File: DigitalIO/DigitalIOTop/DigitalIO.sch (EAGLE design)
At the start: 9 parts, among them K1 HF46105, K2 HF46105, K3 HF46105, K4 HF46105, Q1 691131710002, Q2 691131710002, Q3 691131710002, Q4 691131710002, X1 87438-06

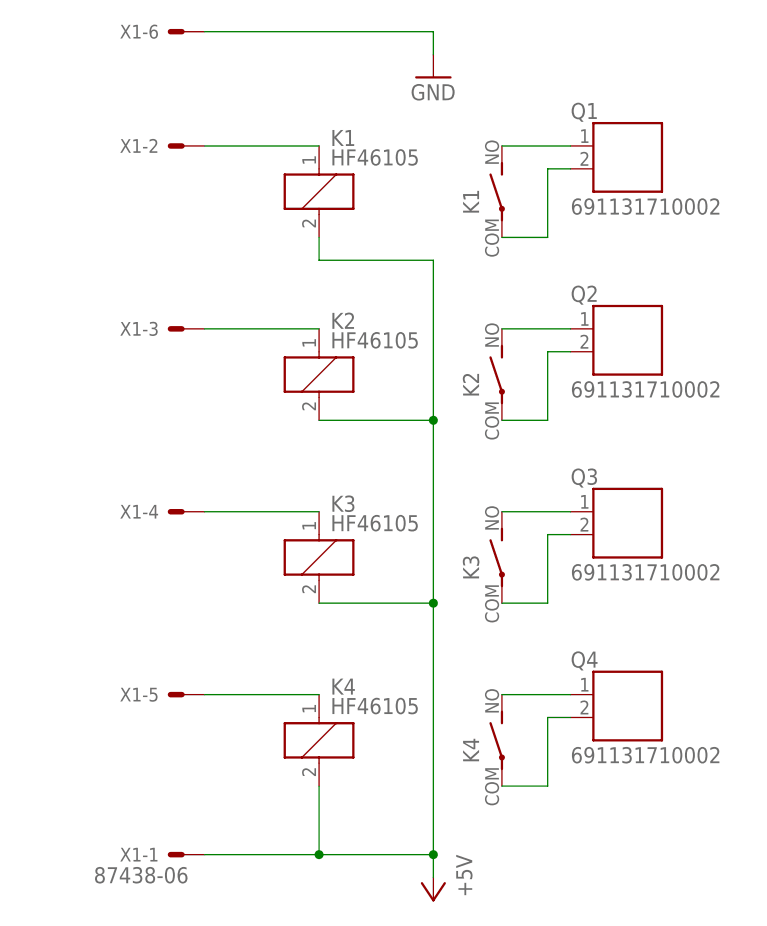
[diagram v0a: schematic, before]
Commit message: Rework to operate with 5V only. Add INT and RESET signals.
Signed-off-by: Alexander Falkenstern <alexander.falkenstern@gmail.com>
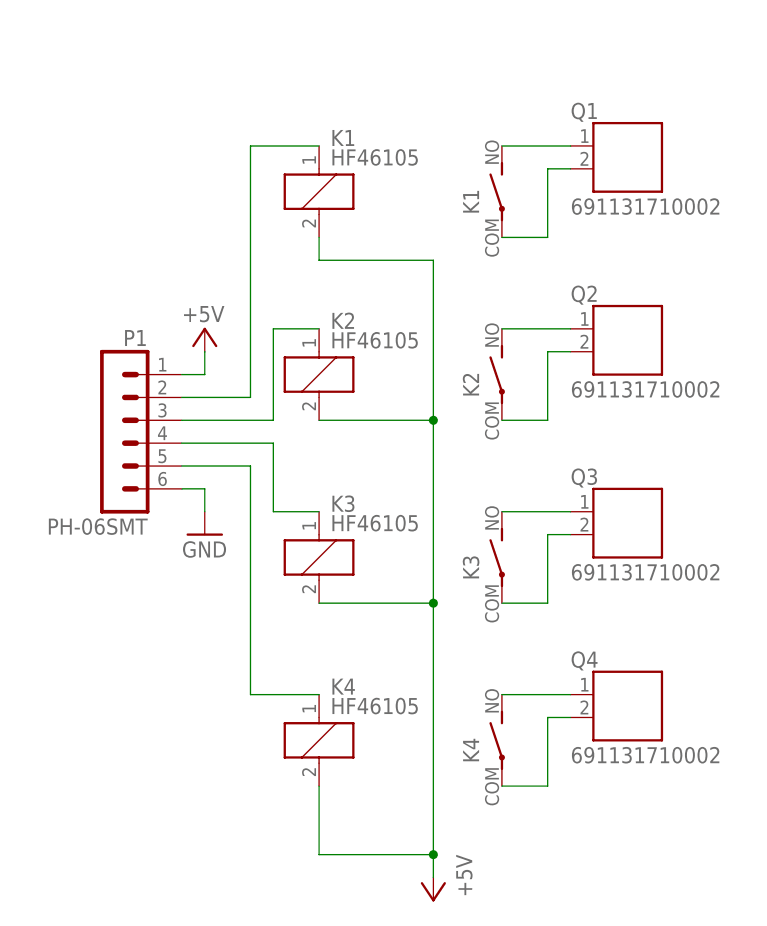
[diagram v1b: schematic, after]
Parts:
- removed X1: 87438-06, con-molex:87438-06
- added P1: PH-06SMT, con-jst-ph:PH-06SMT
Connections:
- net +5V: now also P1.1; no longer X1-1.S
- net GND: now also P1.6; no longer X1-6.S
- net N$14: now also P1.4; no longer X1-4.S
- net N$2: now also P1.3; no longer X1-3.S
- net N$4: now also P1.5; no longer X1-5.S
- net N$5: now also P1.2; no longer X1-2.S
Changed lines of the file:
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@@
 <part name="Q4" library="con-wuerth" deviceset="691131710002" device=""/>
 <part name="GND1" library="supply1" deviceset="GND" device=""/>
-<part name="X1" library="con-molex" deviceset="87438-06" device=""/>
 <part name="P+1" library="supply1" deviceset="+5V" device=""/>
+<part name="P1" library="con-jst-ph" deviceset="PH-06" device="SMT"/>
+<part name="P+2" library="supply1" deviceset="+5V" device=""/>
 </parts>
 <sheets>
@@
 <instance part="Q3" gate="G$1" x="-198.12" y="99.06"/>
 <instance part="Q4" gate="G$1" x="-198.12" y="78.74"/>
-<instance part="GND1" gate="1" x="-213.36" y="147.32"/>
-<instance part="X1" gate="-1" x="-241.3" y="60.96" rot="R180"/>
-<instance part="X1" gate="-2" x="-241.3" y="139.7" rot="R180"/>
-<instance part="X1" gate="-3" x="-241.3" y="119.38" rot="R180"/>
-<instance part="X1" gate="-4" x="-241.3" y="99.06" rot="R180"/>
-<instance part="X1" gate="-5" x="-241.3" y="78.74" rot="R180"/>
-<instance part="X1" gate="-6" x="-241.3" y="152.4" rot="R180"/>
+<instance part="GND1" gate="1" x="-238.76" y="96.52"/>
 <instance part="P+1" gate="1" x="-213.36" y="55.88" rot="R180"/>
+<instance part="P1" gate="G$1" x="-246.38" y="106.68" rot="MR0"/>
+<instance part="P+2" gate="1" x="-238.76" y="119.38" smashed="yes" rot="MR0">
+<attribute name="VALUE" x="-241.3" y="121.92" size="1.778" layer="96" rot="MR180"/>
+</instance>
 </instances>
 <busses>
@@
 <segment>
 <pinref part="K2" gate="1" pin="1"/>
-<wire x1="-226.06" y1="119.38" x2="-238.76" y2="119.38" width="0.1524" layer="91"/>
-<pinref part="X1" gate="-3" pin="S"/>
+<wire x1="-226.06" y1="119.38" x2="-231.14" y2="119.38" width="0.1524" layer="91"/>
+<pinref part="P1" gate="G$1" pin="3"/>
+<wire x1="-231.14" y1="119.38" x2="-231.14" y2="109.22" width="0.1524" layer="91"/>
+<wire x1="-231.14" y1="109.22" x2="-241.3" y2="109.22" width="0.1524" layer="91"/>
 </segment>
 </net>
@@
 <segment>
 <pinref part="K4" gate="1" pin="1"/>
-<wire x1="-226.06" y1="78.74" x2="-238.76" y2="78.74" width="0.1524" layer="91"/>
-<pinref part="X1" gate="-5" pin="S"/>
+<wire x1="-226.06" y1="78.74" x2="-233.68" y2="78.74" width="0.1524" layer="91"/>
+<pinref part="P1" gate="G$1" pin="5"/>
+<wire x1="-233.68" y1="78.74" x2="-233.68" y2="104.14" width="0.1524" layer="91"/>
+<wire x1="-233.68" y1="104.14" x2="-241.3" y2="104.14" width="0.1524" layer="91"/>
 </segment>
 </net>
@@
 <segment>
 <pinref part="K1" gate="1" pin="1"/>
-<wire x1="-226.06" y1="139.7" x2="-238.76" y2="139.7" width="0.1524" layer="91"/>
-<pinref part="X1" gate="-2" pin="S"/>
+<wire x1="-226.06" y1="139.7" x2="-233.68" y2="139.7" width="0.1524" layer="91"/>
+<pinref part="P1" gate="G$1" pin="2"/>
+<wire x1="-233.68" y1="139.7" x2="-233.68" y2="111.76" width="0.1524" layer="91"/>
+<wire x1="-233.68" y1="111.76" x2="-241.3" y2="111.76" width="0.1524" layer="91"/>
 </segment>
 </net>
@@
 <segment>
 <pinref part="K3" gate="1" pin="1"/>
-<wire x1="-238.76" y1="99.06" x2="-226.06" y2="99.06" width="0.1524" layer="91"/>
-<pinref part="X1" gate="-4" pin="S"/>
-</segment>
-</net>
-<net name="GND" class="0">
-<segment>
-<pinref part="GND1" gate="1" pin="GND"/>
-<wire x1="-213.36" y1="149.86" x2="-213.36" y2="152.4" width="0.1524" layer="91"/>
-<wire x1="-213.36" y1="152.4" x2="-238.76" y2="152.4" width="0.1524" layer="91"/>
-<pinref part="X1" gate="-6" pin="S"/>
+<pinref part="P1" gate="G$1" pin="4"/>
+<wire x1="-231.14" y1="99.06" x2="-226.06" y2="99.06" width="0.1524" layer="91"/>
+<wire x1="-231.14" y1="99.06" x2="-231.14" y2="106.68" width="0.1524" layer="91"/>
+<wire x1="-231.14" y1="106.68" x2="-241.3" y2="106.68" width="0.1524" layer="91"/>
 </segment>
 </net>
@@
 <wire x1="-226.06" y1="88.9" x2="-213.36" y2="88.9" width="0.1524" layer="91"/>
 <junction x="-213.36" y="88.9"/>
-<wire x1="-226.06" y1="60.96" x2="-238.76" y2="60.96" width="0.1524" layer="91"/>
-<junction x="-226.06" y="60.96"/>
 <pinref part="K2" gate="1" pin="2"/>
 <wire x1="-226.06" y1="109.22" x2="-213.36" y2="109.22" width="0.1524" layer="91"/>
 <junction x="-213.36" y="109.22"/>
-<pinref part="X1" gate="-1" pin="S"/>
 <pinref part="P+1" gate="1" pin="+5V"/>
 <wire x1="-213.36" y1="60.96" x2="-213.36" y2="58.42" width="0.1524" layer="91"/>
 <junction x="-213.36" y="60.96"/>
 </segment>
+<segment>
+<pinref part="P1" gate="G$1" pin="1"/>
+<wire x1="-241.3" y1="114.3" x2="-238.76" y2="114.3" width="0.1524" layer="91"/>
+<pinref part="P+2" gate="1" pin="+5V"/>
+<wire x1="-238.76" y1="114.3" x2="-238.76" y2="116.84" width="0.1524" layer="91"/>
+</segment>
 </net>
+<net name="GND" class="0">
+<segment>
+<pinref part="P1" gate="G$1" pin="6"/>
+<wire x1="-241.3" y1="101.6" x2="-238.76" y2="101.6" width="0.1524" layer="91"/>
+<pinref part="GND1" gate="1" pin="GND"/>
+<wire x1="-238.76" y1="101.6" x2="-238.76" y2="99.06" width="0.1524" layer="91"/>
+</segment>
+</net>
